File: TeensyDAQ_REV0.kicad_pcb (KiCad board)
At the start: 4 copper layers, 101.6 x 82.6 mm, 105 parts, among them U100 TPS56637RPAR, U101 INA226AIDGSR, U102 BNO055, U103 SN65HVD230DR, U104 DRV5032FBDBZR, Y100 ABS07-32.768KHZ-T

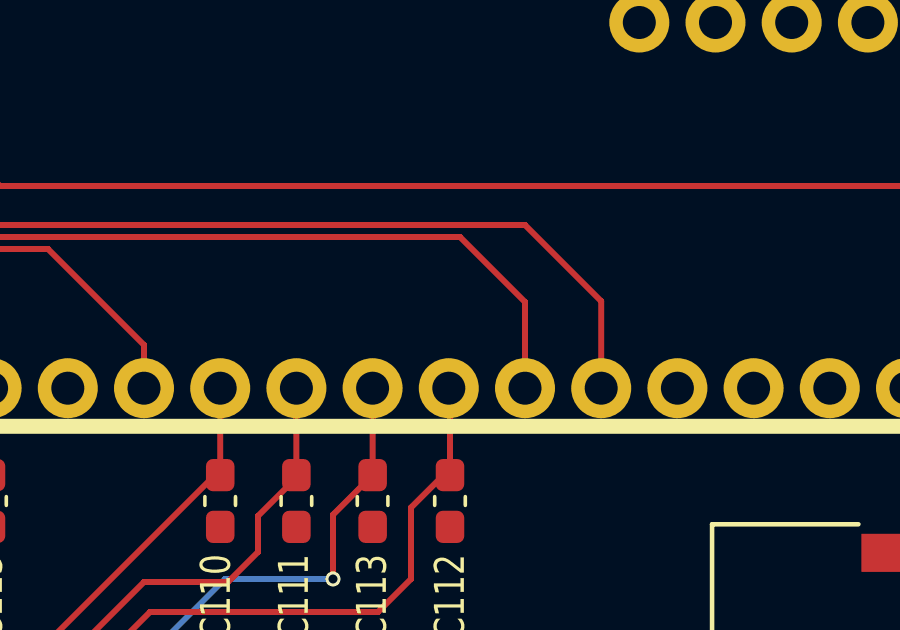
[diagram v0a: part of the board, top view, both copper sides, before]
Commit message: added GND vias to copper pour next to i2c lines to hopefully reduce noise
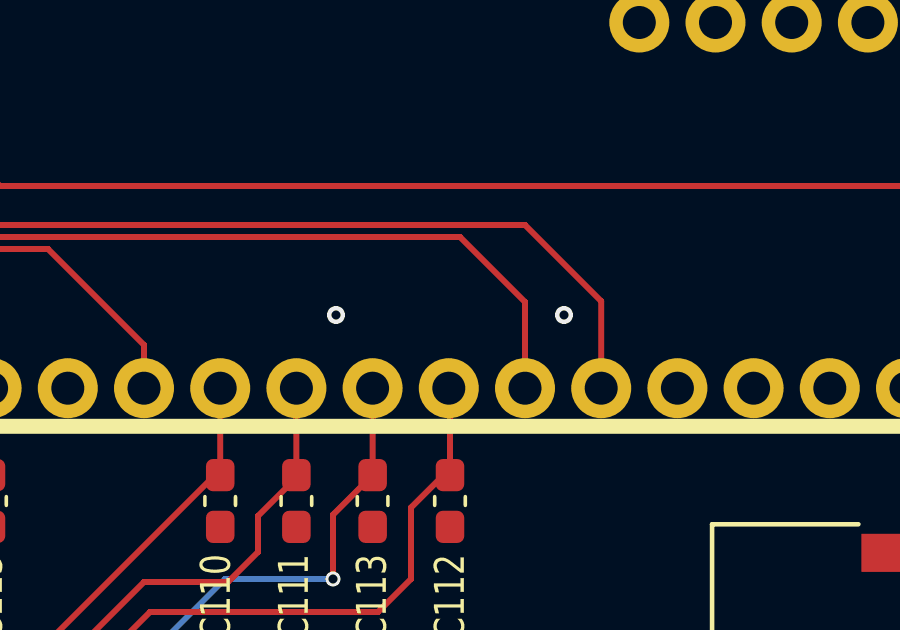
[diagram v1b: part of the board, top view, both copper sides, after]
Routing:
- net GND: vias 7 -> 9
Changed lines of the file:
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@@
 		(tags "test point SMD pad")
 		(property "Reference" "GND"
-			(at -2.85 0 270)
+			(at -2.85 0 -90)
 			(layer "B.SilkS")
 			(effects
@@
 		(tags "test point SMD pad")
 		(property "Reference" "5V"
-			(at 1.95 0 270)
+			(at 1.95 0 -90)
 			(layer "B.SilkS")
 			(effects
@@
 		(tags "test point SMD pad")
 		(property "Reference" "3_T"
-			(at -2.85 -0.1 270)
+			(at -2.85 -0.1 -90)
 			(layer "B.SilkS")
 			(effects
@@
 		(tags "test point SMD pad")
 		(property "Reference" "CANH"
-			(at -2.85 -0.15 270)
+			(at -2.85 -0.15 -90)
 			(layer "B.SilkS")
 			(effects
@@
 		(tags "test point SMD pad")
 		(property "Reference" "GND"
-			(at -2.85 -0.15 270)
+			(at -2.85 -0.15 -90)
 			(layer "B.SilkS")
 			(effects
@@
 		(tags "test point SMD pad")
 		(property "Reference" "5V"
-			(at 1.95 -0.15 270)
+			(at 1.95 -0.15 -90)
 			(layer "B.SilkS")
 			(effects
@@
 		(tags "test point SMD pad")
 		(property "Reference" "GND"
-			(at 1.75 -0.1 270)
+			(at 1.75 -0.1 -90)
 			(layer "B.SilkS")
 			(effects
@@
 		(tags "test point SMD pad")
 		(property "Reference" "CANL"
-			(at 1.95 -0.15 270)
+			(at 1.95 -0.15 -90)
 			(layer "B.SilkS")
 			(effects
@@
 		(tags "test point SMD pad")
 		(property "Reference" "P+"
-			(at -2.85 -0.1 270)
+			(at -2.85 -0.1 -90)
 			(layer "B.SilkS")
 			(effects
@@
 		(tags "test point SMD pad")
 		(property "Reference" "GND"
-			(at -2.85 -0.1 270)
+			(at -2.85 -0.1 -90)
 			(layer "B.SilkS")
 			(effects
@@
 		(tags "test point SMD pad")
 		(property "Reference" "5V"
-			(at 1.95 -0.15 270)
+			(at 1.95 -0.15 -90)
 			(layer "B.SilkS")
 			(effects
@@
 		(tags "test point SMD pad")
 		(property "Reference" "C_T"
-			(at -2.85 -0.1 270)
+			(at -2.85 -0.1 -90)
 			(layer "B.SilkS")
 			(effects
@@
 		(tags "test point SMD pad")
 		(property "Reference" "E_T"
-			(at 1.75 -0.1 270)
+			(at 1.75 -0.1 -90)
 			(layer "B.SilkS")
 			(effects
@@
 		(tags "test point SMD pad")
 		(property "Reference" "B+"
-			(at 1.75 -0.1 270)
+			(at 1.75 -0.1 -90)
 			(layer "B.SilkS")
 			(effects
@@
 		(tags "test point SMD pad")
 		(property "Reference" "GND"
-			(at -2.85 -0.15 270)
+			(at -2.85 -0.15 -90)
 			(layer "B.SilkS")
 			(effects
@@
 		(tags "test point SMD pad")
 		(property "Reference" "D+"
-			(at 1.95 -0.15 270)
+			(at 1.95 -0.15 -90)
 			(layer "B.SilkS")
 			(effects
@@
 		(tags "test point SMD pad")
 		(property "Reference" "P+"
-			(at 1.75 -0.1 270)
+			(at 1.75 -0.1 -90)
 			(layer "B.SilkS")
 			(effects
@@
 		(tags "test point SMD pad")
 		(property "Reference" "D-"
-			(at -2.85 -0.15 270)
+			(at -2.85 -0.15 -90)
 			(layer "B.SilkS")
 			(effects
@@
 		(tags "test point SMD pad")
 		(property "Reference" "GND"
-			(at -2.85 -0.1 270)
+			(at -2.85 -0.1 -90)
 			(layer "B.SilkS")
 			(effects
@@
 	)
 	(via
+		(at 176.4 96.8)
+		(size 0.6)
+		(drill 0.3)
+		(layers "F.Cu" "B.Cu")
+		(free yes)
+		(net 56)
+	)
+	(via
 		(at 129.6 123.8)
 		(size 0.6)
@@
 		(net 56)
 	)
+	(via
+		(at 168.8 96.8)
+		(size 0.6)
+		(drill 0.3)
+		(layers "F.Cu" "B.Cu")
+		(free yes)
+		(net 56)
+	)

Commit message: changed date lol
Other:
- board text added: "CHARLIE MILLHOLLIN 2-11-2025"
- board text removed: "CHARLIE MILLHOLLIN 2-10-2025"

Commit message: added TVS diodes to external pins for protection. Ran fabrication output. Ran iBOM generation. All part links can be seen in the iBOM. Download and open to see this
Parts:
- removed 3_T, C_T, D+, D-, E_T, H1, H2, I/O_1, I/O_2, VD_1: TestPoint, TestPoint:TestPoint_Pad_D1.0mm
- added D104: SMAJ5.0A, Diode_SMD:D_SMA, F.Cu at (178.8, 71.7)
- added D105: SMAJ5.0A, Diode_SMD:D_SMA, F.Cu at (175.7, 59.7)
- added D106: SMAJ5.0A, Diode_SMD:D_SMA, F.Cu at (147.0, 61.8)
- added D107: SMAJ5.0A, Diode_SMD:D_SMA, F.Cu at (134.6, 61.8)
- added D108: SMAJ5.0A, Diode_SMD:D_SMA, F.Cu at (175.7, 56.2)
- added D109: SMAJ5.0A, Diode_SMD:D_SMA, F.Cu at (183.4, 71.6)
- added D110: SMAJ5.0A, Diode_SMD:D_SMA, F.Cu at (140.2, 123.8)
- added D111: SMAJ5.0A, Diode_SMD:D_SMA, F.Cu at (147.2, 123.8)
- added D112: SMAJ5.0A, Diode_SMD:D_SMA, F.Cu at (143.7, 123.8)
- added D113: SMAJ5.0A, Diode_SMD:D_SMA, F.Cu at (136.7, 123.8)
- added D115: SMAJ5.0A, Diode_SMD:D_SMA, F.Cu at (150.7, 123.8)
- CANH, CANL: moved to F.Cu
- moved CANL 5.86 mm to (119.0, 53.6), turned to 0 degrees
- moved CANH 5.10 mm to (119.0, 56.6), turned to 0 degrees
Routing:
- net GND: track 25.2 -> 10.9 mm
- net /Enclosure Connectors/P2: track 46.9 -> 32.6 mm
- net /CAN/CANH: track 59.1 -> 46.0 mm
- net /Analog/VDIV1_u: track 61.4 -> 72.8 mm, vias 0 -> 2
- net /Enclosure Connectors/USB_D-: track 135.6 -> 124.3 mm, vias 0 -> 1
- net /Analog/Engine_Thermistor+: track 71.3 -> 82.0 mm, vias 0 -> 2
- net /Analog/VMeas_BATu: track 42.7 -> 51.6 mm, vias 2 -> 3
- net /Analog/Hall_Signal1: track 106.1 -> 97.4 mm
- net /Analog/Thermistor3_u: track 103.7 -> 99.1 mm, vias 2 -> 4
- net /Enclosure Connectors/P1: track 28.1 -> 23.8 mm
- net /Analog/VDIV1+: track 25.4 -> 21.1 mm
- net /CAN/CANL: track 44.7 -> 41.6 mm
- net /Enclosure Connectors/USB_D+: track 113.0 -> 114.9 mm, vias 0 -> 1
- net RTC_BAT+: track 98.3 -> 96.6 mm
- net /Analog/CVT_Thermistor+: track 96.8 -> 95.3 mm, vias 0 -> 2
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
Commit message: updated QR code to match github repository on silkscreen
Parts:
- added G***: LOGO, qr:teensyDAQ_QR, B.Cu at (190.5, 59.3)

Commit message: added power planes to correct layer. Added 10A 1206 fuse to battery input before current measurement resistor and reverse polarity diode
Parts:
- added F100: Fuse, Fuse:Fuse_1206_3216Metric, F.Cu at (113.5, 108.2)
- moved D103 2.35 mm to (125.7, 108.3)
- moved R127 0.80 mm to (118.2, 108.3)
- moved 5V103 0.70 mm to (164.0, 127.1)
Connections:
- B+ pad 1: CUR_S_+ -> /Analog/Battery_IN+
- J100 pad 13: CUR_S_+ -> /Analog/Battery_IN+
- R117 pad 2: CUR_S_+ -> /Analog/Battery_IN+
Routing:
- net +5V: track 168.9 -> 67.8 mm, vias 1 -> 6
- net /Enclosure Connectors/Power_OUT+: track 97.7 -> 17.1 mm
- net CUR_S_+: track 52.9 -> 9.66 mm
- net /Analog/Battery_IN+: track 0.00 -> 38.3 mm, vias 0 -> 1
- net /CAN/CANL: track 41.6 -> 44.9 mm
- net /CAN/CANH: track 46.0 -> 49.3 mm
- net CUR_S_-: track 10.1 -> 7.27 mm
- added copper zone on In2.Cu, net +5V
- added copper zone on In2.Cu, net /Enclosure Connectors/Power_OUT+

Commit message: updated QR code
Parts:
- removed the G*** at (190.5, 59.3)
- added G***: LOGO, qr:TeensyDAQ_Hardware_QR, B.Cu at (190.7, 59.4)
